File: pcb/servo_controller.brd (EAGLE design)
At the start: 68.6 x 53.3 mm, 55 parts, among them IC1 PIC18F452, IC2 LM2936MP-3.0, Q1 10Mhz, U1 ARDUINOR3-DIMENSION

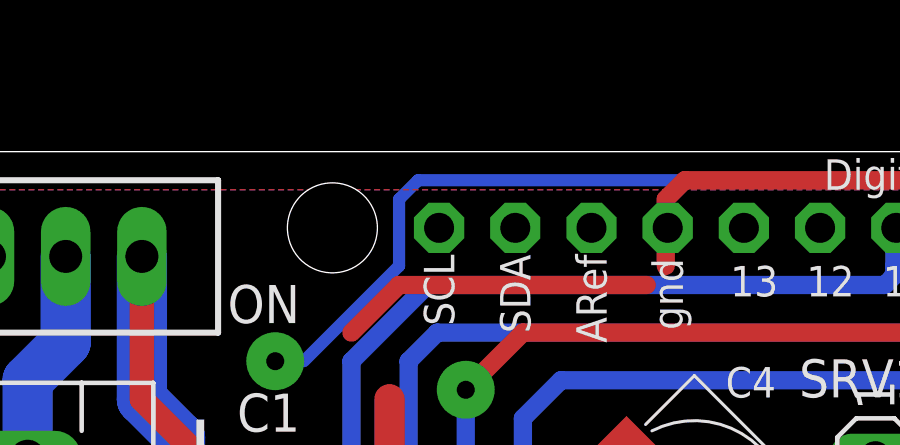
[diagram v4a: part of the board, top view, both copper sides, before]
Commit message: Added sot23 footprint for max4173
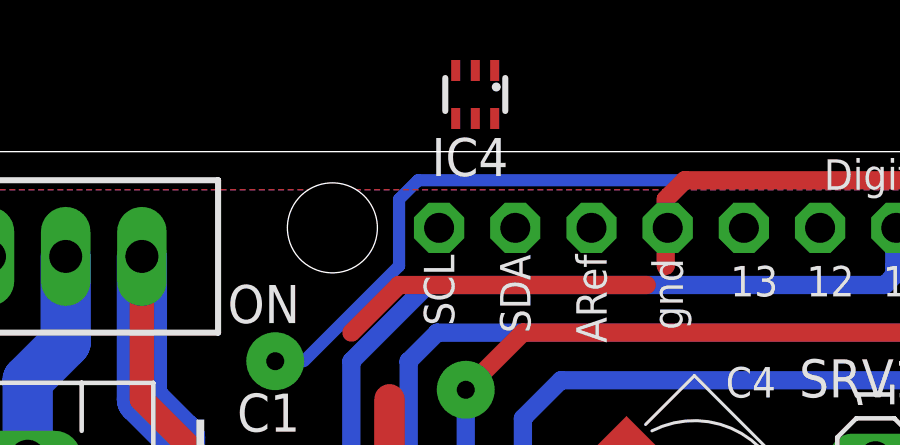
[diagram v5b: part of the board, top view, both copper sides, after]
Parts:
- added IC4: (no value), AWJLEagleLib:SOT-363
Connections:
- net +5V: now also IC4.3
- net SERVO_CURRENT: now also IC4.6
- net VDD: now also IC4.4
- net VEE: now also IC4.5
- net VSS: now also IC4.1
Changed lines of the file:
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@@
 <attribute name="VALUE" x="11.43" y="54.9275" size="1.778" layer="27" rot="R180"/>
 </element>
+<element name="IC4" library="AWJLEagleLib" package="SOT-363" value="" x="20.0025" y="55.245" rot="R180"/>
 </elements>
 <signals>
@@
 <wire x1="41.0875" y1="13.6525" x2="40.9575" y2="13.5225" width="0.6096" layer="1"/>
 <via x="53.34" y="8.255" extent="1-16" drill="0.6" diameter="1.9304"/>
+<contactref element="IC4" pad="1"/>
+<wire x1="5.3213" y1="23.1775" x2="20.6525" y2="56.045" width="0" layer="19" extent="1-1"/>
 <wire x1="45.24375" y1="17.93875" x2="45.24375" y2="18.33625" width="0" layer="19" extent="1-1"/>
 </signal>
@@
 <wire x1="36.5125" y1="8.255" x2="39.4275" y2="8.255" width="0.6096" layer="1"/>
 <via x="36.5125" y="8.255" extent="1-16" drill="0.6" diameter="1.9304"/>
+<contactref element="IC4" pad="3"/>
+<wire x1="7.9375" y1="26.3525" x2="19.3525" y2="56.045" width="0" layer="19" extent="1-1"/>
 </signal>
 <signal name="VDD">
@@
 <wire x1="11.43" y1="42.545" x2="8.89" y2="45.085" width="0.8128" layer="1"/>
 <wire x1="8.89" y1="45.085" x2="8.89" y2="49.8475" width="0.8128" layer="1"/>
+<contactref element="IC4" pad="4"/>
 <wire x1="18.415" y1="27.9908" x2="18.415" y2="27.7525" width="0" layer="19" extent="1-1"/>
+<wire x1="19.3525" y1="54.445" x2="8.5725" y2="19.05" width="0" layer="19" extent="1-16"/>
 </signal>
 <signal name="N$7">
@@
 <contactref element="C4" pad="+"/>
 <contactref element="C5" pad="+"/>
+<contactref element="IC4" pad="5"/>
 <wire x1="29.21" y1="39.785884375" x2="29.00205625" y2="39.577940625" width="0" layer="19" extent="1-1"/>
 <wire x1="18.415" y1="18.6025" x2="18.415" y2="19.05" width="0" layer="19" extent="1-1"/>
 <wire x1="19.79455625" y1="14.07955625" x2="19.25794375" y2="14.39705625" width="0" layer="19" extent="1-1"/>
+<wire x1="20.0025" y1="54.445" x2="10.5537" y2="23.1775" width="0" layer="19" extent="1-1"/>
 </signal>
 <signal name="SERVO_CURRENT">
@@
 <contactref element="D2" pad="3"/>
 <wire x1="6.985" y1="20.0025" x2="5.2275" y2="20.0025" width="0.6096" layer="1"/>
+<contactref element="IC4" pad="6"/>
+<wire x1="6.985" y1="21.59" x2="20.6525" y2="54.445" width="0" layer="19" extent="1-1"/>
 </signal>
 <signal name="N$20">

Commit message: Misc
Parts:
- IC3: value (none) -> MAX4173FESA+
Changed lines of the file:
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@@
 <attribute name="VALUE" x="16.1925" y="6.6675" size="1.27" layer="27" rot="R90"/>
 </element>
-<element name="IC3" library="AWJLEagleLib" package="SO08" value="" x="7.9375" y="23.8125" rot="R270"/>
+<element name="IC3" library="AWJLEagleLib" package="SO08" value="MAX4173FESA+" x="7.9375" y="23.8125" rot="R270"/>
 <element name="RESET" library="testpad" package="TP20R" value="TPTP20R" x="44.45" y="19.05" smashed="yes" rot="MR270">
 <attribute name="TP_SIGNAL_NAME" value="" x="46.99" y="19.05" size="1" layer="38" rot="MR270"/>
@@
 <via x="53.34" y="8.255" extent="1-16" drill="0.6" diameter="1.9304"/>
 <contactref element="IC4" pad="1"/>
-<wire x1="5.3213" y1="23.1775" x2="20.6525" y2="56.045" width="0" layer="19" extent="1-1"/>
+<wire x1="18.0975" y1="52.3875" x2="20.6525" y2="56.045" width="0" layer="19" extent="1-16"/>
 <wire x1="45.24375" y1="17.93875" x2="45.24375" y2="18.33625" width="0" layer="19" extent="1-1"/>
 </signal>
@@
 <via x="36.5125" y="8.255" extent="1-16" drill="0.6" diameter="1.9304"/>
 <contactref element="IC4" pad="3"/>
-<wire x1="7.9375" y1="26.3525" x2="19.3525" y2="56.045" width="0" layer="19" extent="1-1"/>
+<wire x1="10.4775" y1="29.21" x2="19.3525" y2="56.045" width="0" layer="19" extent="1-1"/>
 </signal>
 <signal name="VDD">
@@
 <wire x1="8.89" y1="45.085" x2="8.89" y2="49.8475" width="0.8128" layer="1"/>
 <contactref element="IC4" pad="4"/>
-<wire x1="18.415" y1="27.9908" x2="18.415" y2="27.7525" width="0" layer="19" extent="1-1"/>
-<wire x1="19.3525" y1="54.445" x2="8.5725" y2="19.05" width="0" layer="19" extent="1-16"/>
+<wire x1="8.89" y1="49.8475" x2="19.3525" y2="54.445" width="0" layer="19" extent="1-1"/>
+<wire x1="18.415" y1="27.7525" x2="18.415" y2="27.9908" width="0" layer="19" extent="1-1"/>
 </signal>
 <signal name="N$7">
@@
 <contactref element="C5" pad="+"/>
 <contactref element="IC4" pad="5"/>
-<wire x1="29.21" y1="39.785884375" x2="29.00205625" y2="39.577940625" width="0" layer="19" extent="1-1"/>
+<wire x1="29.21" y1="40.64" x2="20.0025" y2="54.445" width="0" layer="19" extent="1-16"/>
+<wire x1="29.00205625" y1="39.577940625" x2="29.21" y2="39.785884375" width="0" layer="19" extent="1-1"/>
 <wire x1="18.415" y1="18.6025" x2="18.415" y2="19.05" width="0" layer="19" extent="1-1"/>
 <wire x1="19.79455625" y1="14.07955625" x2="19.25794375" y2="14.39705625" width="0" layer="19" extent="1-1"/>
-<wire x1="20.0025" y1="54.445" x2="10.5537" y2="23.1775" width="0" layer="19" extent="1-1"/>
 </signal>
 <signal name="SERVO_CURRENT">
@@
 <wire x1="6.985" y1="20.0025" x2="5.2275" y2="20.0025" width="0.6096" layer="1"/>
 <contactref element="IC4" pad="6"/>
-<wire x1="6.985" y1="21.59" x2="20.6525" y2="54.445" width="0" layer="19" extent="1-1"/>
+<wire x1="6.6675" y1="21.9075" x2="20.6525" y2="54.445" width="0" layer="19" extent="1-1"/>
 </signal>
 <signal name="N$20">

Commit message: Elec
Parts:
- removed IC4: (no value), AWJLEagleLib:SOT-363
- added U$2: (no value), ohw-logo:OSHW_8X350_NOTEXT
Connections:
- net +5V: no longer IC4.3
- net SERVO_CURRENT: no longer IC4.6
- net VDD: no longer IC4.4
- net VEE: no longer IC4.5
- net VSS: no longer IC4.1
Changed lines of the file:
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@@
 <hole x="15.24" y="50.8" drill="3"/>
 <text x="11.7475" y="47.625" size="1.27" layer="25">ON</text>
-<text x="43.4975" y="46.0375" size="2.1844" layer="25">Bleuette</text>
+<text x="40.3225" y="46.0375" size="2.1844" layer="25">Bleuette</text>
 <text x="54.61" y="33.9725" size="2.1844" layer="26" rot="MR0">Bleuette</text>
 <text x="54.61" y="31.75" size="1.778" layer="26" rot="MR0">Servo controller</text>
@@
 <attribute name="VALUE" x="11.43" y="54.9275" size="1.778" layer="27" rot="R180"/>
 </element>
-<element name="IC4" library="AWJLEagleLib" package="SOT-363" value="" x="20.0025" y="55.245" rot="R180"/>
+<element name="U$2" library="ohw-logo" package="OSHW_8X350_NOTEXT" value="" x="56.8325" y="20.955" rot="MR0"/>
 </elements>
 <signals>
@@
 <wire x1="41.0875" y1="13.6525" x2="40.9575" y2="13.5225" width="0.6096" layer="1"/>
 <via x="53.34" y="8.255" extent="1-16" drill="0.6" diameter="1.9304"/>
-<contactref element="IC4" pad="1"/>
-<wire x1="18.0975" y1="52.3875" x2="20.6525" y2="56.045" width="0" layer="19" extent="1-16"/>
 <wire x1="45.24375" y1="17.93875" x2="45.24375" y2="18.33625" width="0" layer="19" extent="1-1"/>
 </signal>
@@
 <wire x1="36.5125" y1="8.255" x2="39.4275" y2="8.255" width="0.6096" layer="1"/>
 <via x="36.5125" y="8.255" extent="1-16" drill="0.6" diameter="1.9304"/>
-<contactref element="IC4" pad="3"/>
-<wire x1="10.4775" y1="29.21" x2="19.3525" y2="56.045" width="0" layer="19" extent="1-1"/>
 </signal>
 <signal name="VDD">
@@
 <wire x1="11.43" y1="42.545" x2="8.89" y2="45.085" width="0.8128" layer="1"/>
 <wire x1="8.89" y1="45.085" x2="8.89" y2="49.8475" width="0.8128" layer="1"/>
-<contactref element="IC4" pad="4"/>
-<wire x1="8.89" y1="49.8475" x2="19.3525" y2="54.445" width="0" layer="19" extent="1-1"/>
-<wire x1="18.415" y1="27.7525" x2="18.415" y2="27.9908" width="0" layer="19" extent="1-1"/>
+<wire x1="18.415" y1="27.9908" x2="18.415" y2="27.7525" width="0" layer="19" extent="1-1"/>
 </signal>
 <signal name="N$7">
@@
 <contactref element="C4" pad="+"/>
 <contactref element="C5" pad="+"/>
-<contactref element="IC4" pad="5"/>
-<wire x1="29.21" y1="40.64" x2="20.0025" y2="54.445" width="0" layer="19" extent="1-16"/>
-<wire x1="29.00205625" y1="39.577940625" x2="29.21" y2="39.785884375" width="0" layer="19" extent="1-1"/>
+<wire x1="29.21" y1="39.785884375" x2="29.00205625" y2="39.577940625" width="0" layer="19" extent="1-1"/>
 <wire x1="18.415" y1="18.6025" x2="18.415" y2="19.05" width="0" layer="19" extent="1-1"/>
 <wire x1="19.79455625" y1="14.07955625" x2="19.25794375" y2="14.39705625" width="0" layer="19" extent="1-1"/>
@@
 <contactref element="D2" pad="3"/>
 <wire x1="6.985" y1="20.0025" x2="5.2275" y2="20.0025" width="0.6096" layer="1"/>
-<contactref element="IC4" pad="6"/>
-<wire x1="6.6675" y1="21.9075" x2="20.6525" y2="54.445" width="0" layer="19" extent="1-1"/>
 </signal>
 <signal name="N$20">
